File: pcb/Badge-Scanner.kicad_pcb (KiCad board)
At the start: 2 copper layers, 73 x 52 mm, 63 parts, among them J1 I2C, J2 NFC-Module, J4 Micro_SD_Card_Det1, J5 Serial, Q1 AO3400A, Q2 AO3401A, Q3 AO3400A, Q4 AO3401A, Q5 AO3400A, Q6 AO3401A, SW1 Power, U1 Pico W, U2 DS3231MZ, U3 TP4056

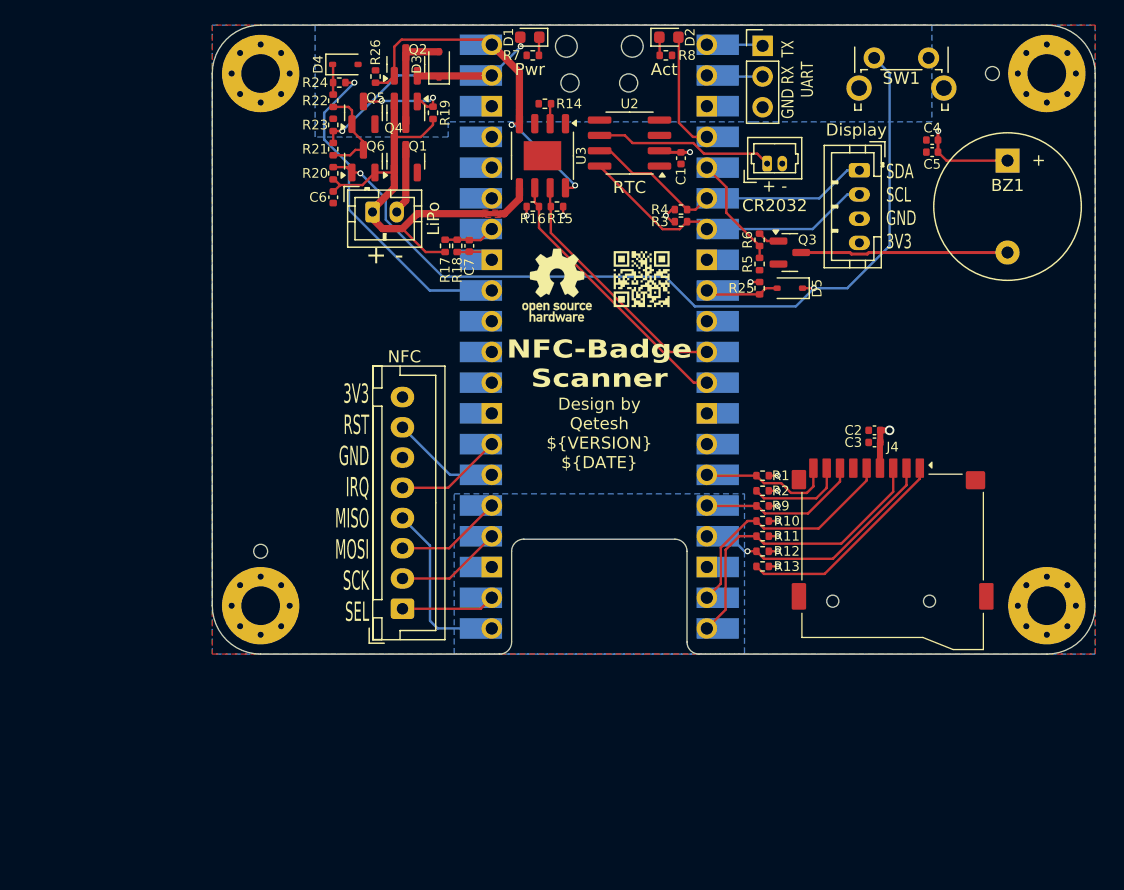
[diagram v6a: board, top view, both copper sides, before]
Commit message: fix: add FET to measurement circuit
Disable the battery measurement circuit when the device is switched off to save energy
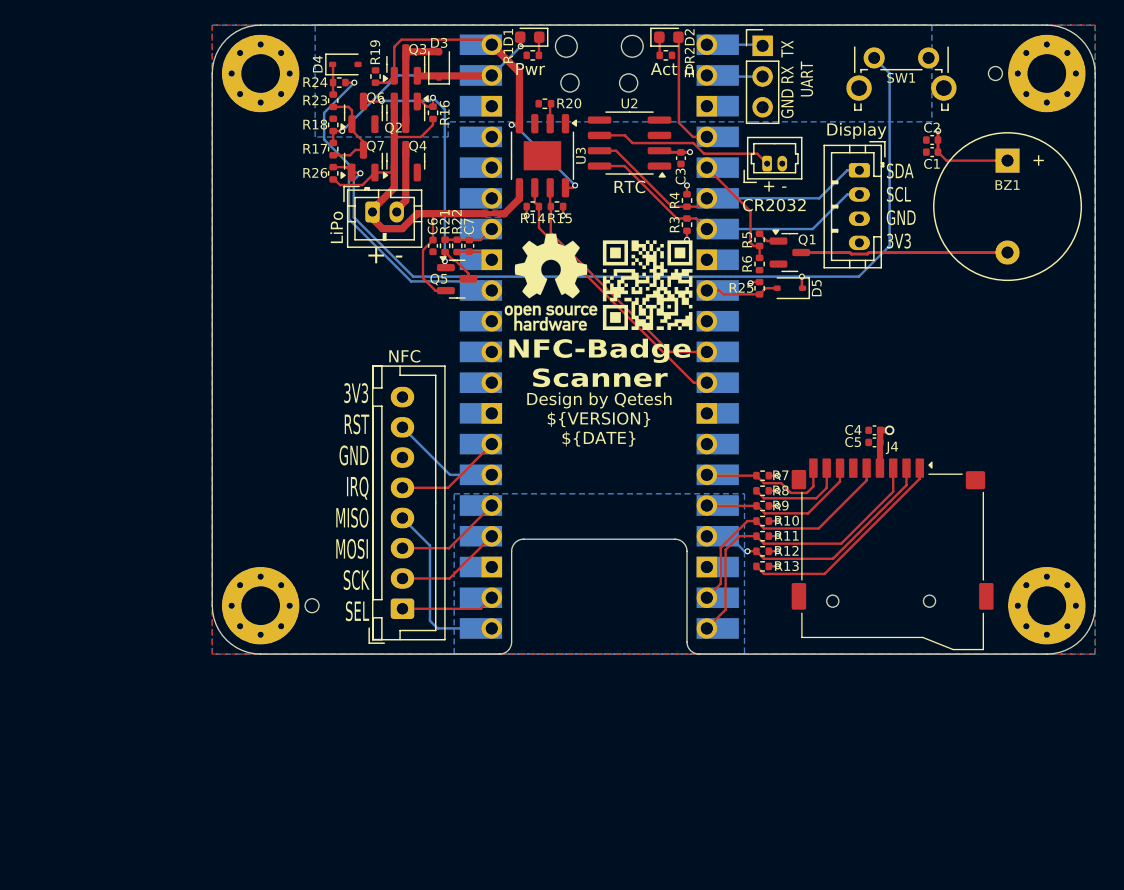
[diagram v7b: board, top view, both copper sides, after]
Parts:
- removed the G*** at (128.5, 95.2)
- removed the REF** at (121.5, 95.8)
- added G***: LOGO, My_Footprints:qr_qete.sh-el_08, F.Cu at (129.0, 95.8)
- added Q5: AO3401A, Package_TO_SOT_SMD:SOT-23, F.Cu at (113.2, 95.2)
- added REF**: OSHW-Logo_7.5x8mm_SilkScreen, Symbol:OSHW-Logo_7.5x8mm_SilkScreen, F.Cu at (121.0, 95.5)
- R21: renamed from R17; value 10M -> 1M
- R22: renamed from R18; value 10M -> 1M
- moved C6 9.18 mm to (111.2, 92.5)
- moved REF** 6.19 mm to (101.2, 122.2)
- moved R4 0.90 mm to (132.2, 88.8), turned to 90 degrees
- moved R3 0.56 mm to (132.2, 90.8), turned to -90 degrees
- moved REF** 0.25 mm to (157.8, 78.2)
- renumbered C5 to C1, C4 to C2, C1 to C3, C2 to C4, C3 to C5, J2 to J1, J5 to J2, J1 to J3, Q3 to Q1, Q4 to Q2, Q2 to Q3, Q1 to Q4, Q5 to Q6, Q6 to Q7, R7 to R1, R16 to R14, R19 to R16, R21 to R17, R23 to R18, R26 to R19, R8 to R2, R14 to R20, R22 to R23, R20 to R26, R6 to R5, R5 to R6, R1 to R7, R2 to R8
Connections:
- net /BattMeas renamed /BattVolt
- net /~{PwrButton} renamed /~{Button}
- R21 pad 1: /Battery Management/Batt+ -> Net-(Q5-D)
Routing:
- net /Battery Management/BattSwG: track 8.10 -> 22.6 mm, vias 2 -> 3
- net Net-(Q5-D): track 0.00 -> 3.13 mm
- net /Battery Management/Batt+: track 39.7 -> 42.5 mm
- net /SCL: track 25.3 -> 24.8 mm
- net +3V3: track 23.6 -> 23.3 mm, vias 14 -> 15
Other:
- board text added: "0>UART0 TX 1<UART0 RX 2>LED 3>Buzzer 4=I2C0 SDA 5>I2C0 SCL 6<~{Button} 8<~{Charge Active} 9<~{Charge Standby} 27>~{Power Off} 28<Battery Voltage"
- board text added: "SD-Card SPI1 11 DETECT 12 MISO 13 CS 14 SCK 15 MOSI NFC SPI0 16 MISO 17 CS 18 SCK 19 MOSI 20 RST 21 IRQ"
- board text removed: "0 UART TX 1 UART RX 2 LED 3 Buzzer 4 I2C SDA 5 I2C SDL 6 Power Button 8 Charge Active 9 Charge Standby 27 Power Off 28 Battery Voltage"
- board text removed: "11 SD DET 12 SD MISO 13 SD CS 14 SD SCK 15 SD MOSI 16 NFC MISO 17 NFC CS 18 NFC SCK 19 NFC MOSI 20 NFC RST 21 NFC IRQ"

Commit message: fix: power switch circuit capacitance
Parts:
- removed the D4 at (104.0, 77.5)
- removed the R18 at (103.0, 82.5)
- removed the R24 at (103.5, 79.0)
- added C8: 10u, Capacitor_SMD:C_0402_1005Metric, F.Cu at (103.0, 76.5)
- added Q8: AO3400A, Package_TO_SOT_SMD:SOT-23, F.Cu at (105.5, 85.5)
- added R25: 10k, Resistor_SMD:R_0402_1005Metric, F.Cu at (103.0, 86.5)
- R22: renamed from R23; value 10k -> 1k
- moved R17 6.00 mm to (103.0, 78.5), turned to 90 degrees
- moved Q6 4.00 mm to (105.5, 77.5)
- moved Q7 4.00 mm to (105.5, 81.5)
- moved R22 4.00 mm to (103.0, 84.5)
- moved R24 4.00 mm to (103.0, 82.5)
- moved R18 3.91 mm to (108.2, 75.0), turned to 180 degrees
- renumbered D5 to D4, Q5 to Q4, Q4 to Q5, R19 to R18, R20 to R19, R21 to R20, R22 to R21, R25 to R23, R26 to R24
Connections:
- Q7 pad 2: /Battery Management/Batt+ -> Net-(Q7-S)
- R22 pad 1: /Battery Management/BattSw -> /Battery Management/Batt+
- R22 pad 2: Net-(D4-K) -> Net-(Q7-S)
- R24 pad 1: /Battery Management/Batt+ -> Net-(Q7-S)
- U1 pad 32: /~{BattPwrOff} -> /BattPwrOff
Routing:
- net /~{BattPwrOff}: track 28.2 -> 0.00 mm, vias 1 -> 0
- net /BattPwrOff: track 0.00 -> 20.1 mm, vias 0 -> 1
- net Net-(Q7-S): track 0.00 -> 4.75 mm
- net /Battery Management/SW1: track 70.8 -> 74.8 mm
- net /Battery Management/BattSw: track 7.91 -> 11.0 mm
- net /Battery Management/BattSwG: track 22.6 -> 25.6 mm
- net VSYS: track 26.3 -> 23.7 mm
- net Net-(D4-K): track 2.52 -> 0.00 mm
- net VBUS: track 29.0 -> 27.8 mm
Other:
- board text added: "0>UART0 TX 1<UART0 RX 2>LED 3>Buzzer 4=I2C0 SDA 5>I2C0 SCL 6<~{Button} 8<~{Charge Active} 9<~{Charge Standby} 27>Power Off 28<Battery Voltage"
- board text removed: "0>UART0 TX 1<UART0 RX 2>LED 3>Buzzer 4=I2C0 SDA 5>I2C0 SCL 6<~{Button} 8<~{Charge Active} 9<~{Charge Standby} 27>~{Power Off} 28<Battery Voltage"
